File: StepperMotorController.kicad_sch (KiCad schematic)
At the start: 16 parts, among them J1 Conn_01x04, J2 Conn_01x04, J3 Conn_01x08, J4 Conn_01x02, M1 Mounting_Hole, M2 Mounting_Hole, M3 Mounting_Hole, M4 Mounting_Hole, U1 ACS725xLCTR-10AU

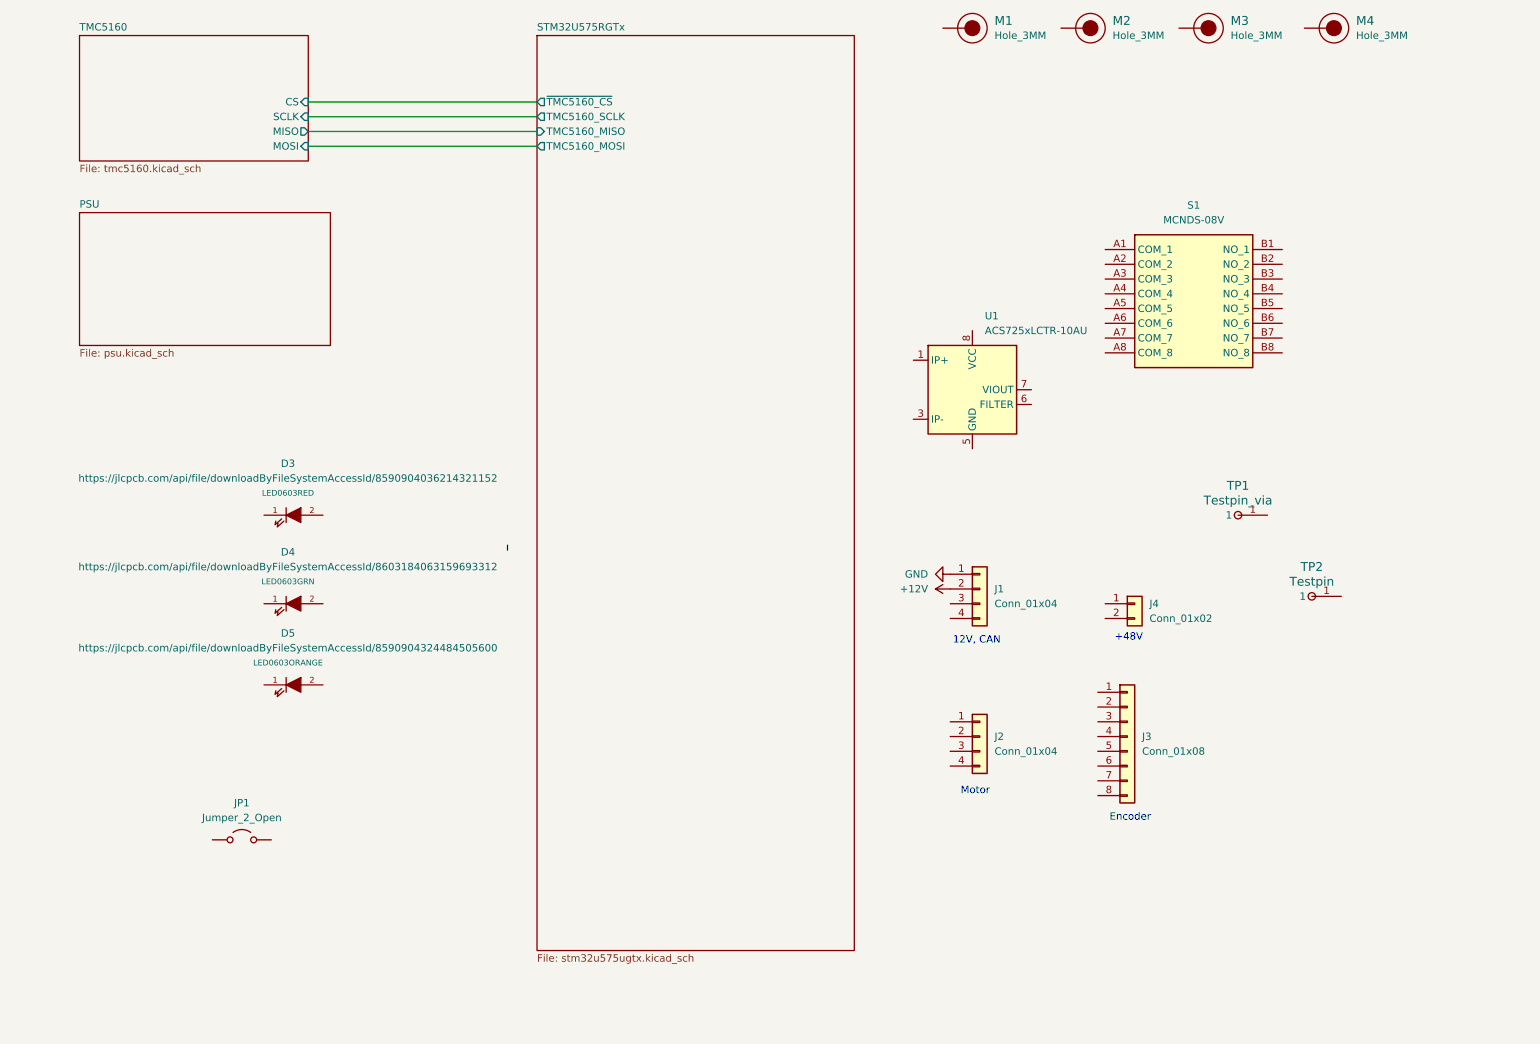
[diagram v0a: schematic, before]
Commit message: PCB 3mm free space around edges, 9pin dipswitch, re-arragnged components
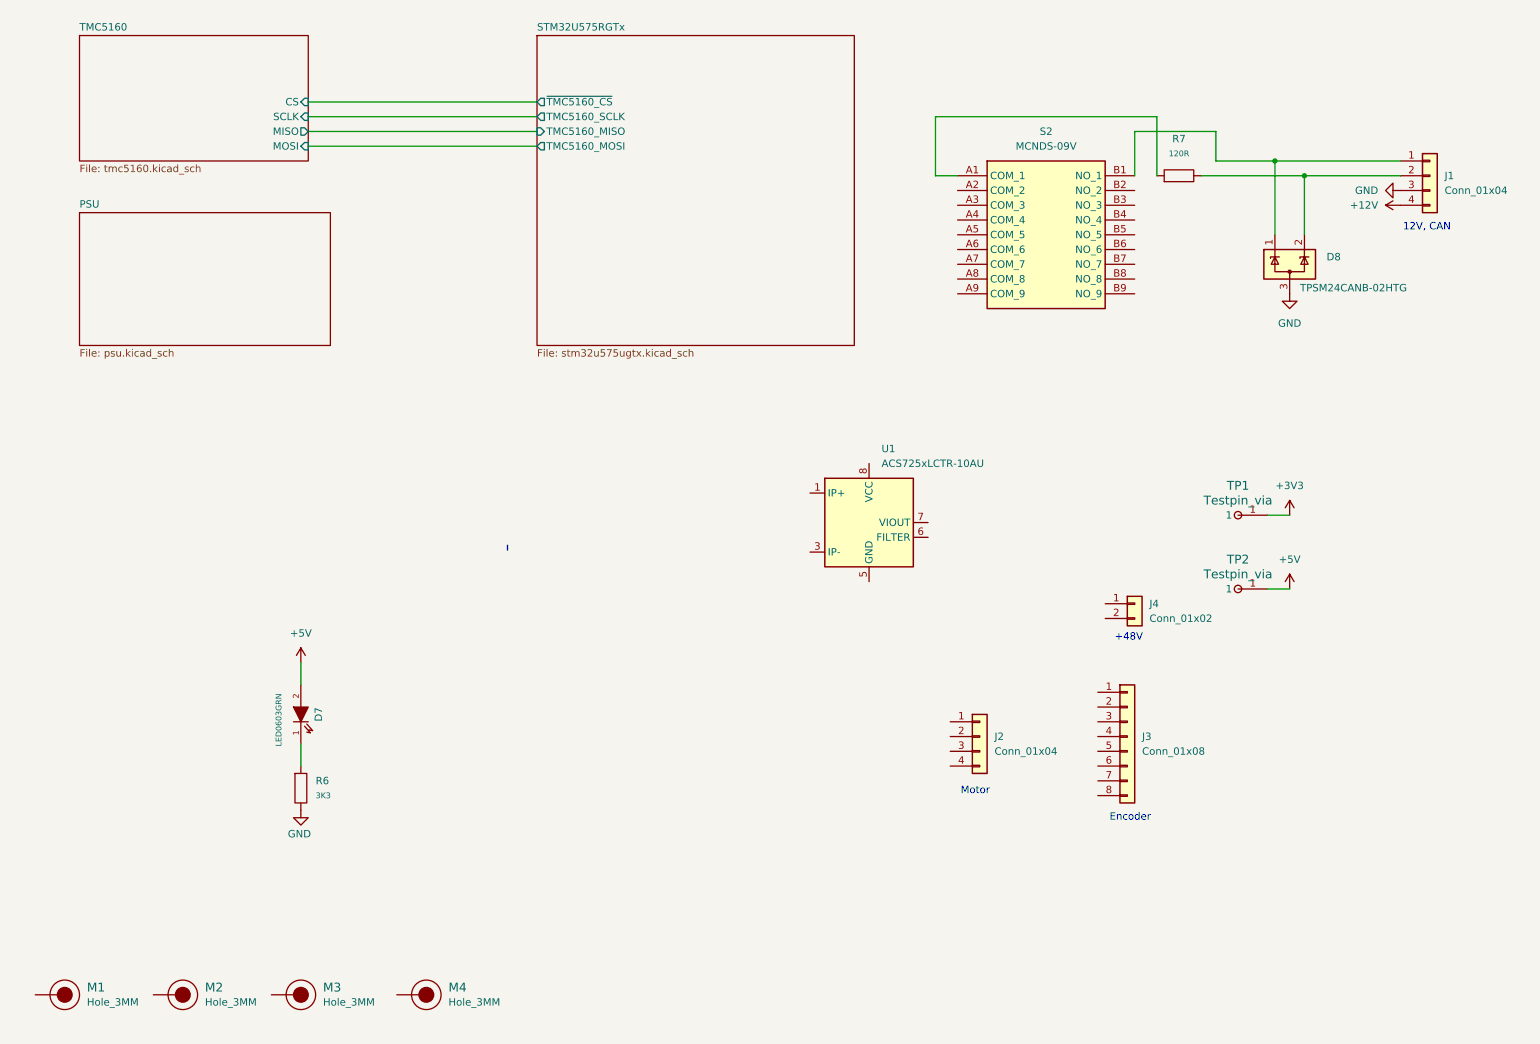
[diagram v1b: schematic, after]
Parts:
- removed D3: LED0603RED_APT1608EC, D&R_Discrete:LED_0603_1608Metric, symbol Doggen:LED0603RED_APT1608EC
- removed D4: LED0603GRN_APT1608ZGC, D&R_Discrete:LED_0603_1608Metric, symbol Doggen:LED0603GRN_APT1608ZGC
- removed D5: LED0603ORANGE_APT1608SECK, D&R_Discrete:LED_0603_1608Metric, symbol Doggen:LED0603ORANGE_APT1608SECK
- removed JP1: Jumper_2_Open, Connector_PinHeader_2.54mm:PinHeader_1x02_P2.54mm_Vertical, symbol Jumper:Jumper_2_Open
- removed S1: MCNDS-08V, Doggen:MCNDS08V, symbol Doggen:MCNDS-08V
- removed TP2: Testpin, D&R_Other:TP1mm, symbol D&R_other:Testpin
- added D7: LED0603GRN_APT1608ZGC, D&R_Discrete:LED_0603_1608Metric, symbol Doggen:LED0603GRN_APT1608ZGC
- added D8: TPSM24CANB-02HTG, Package_TO_SOT_SMD:SOT-23-3, symbol Doggen:TPSM24CANB-02HTG
- added R6: 3K3#0603, D&R_Passive:R_0603, symbol D&R_Passive:3K3#0603
- added R7: 120R#0603, D&R_Passive:R_0603, symbol D&R_Passive:120R#0603
- added S2: MCNDS-09V, MCNDS09V, symbol Doggen:MCNDS-09V
- added TP2: Testpin_via, D&R_Other:Testpoint_Via, symbol D&R_other:Testpin_via
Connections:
- net +12V: now also J1.4 (Pin_4); no longer J1.2 (Pin_2)
- net GND: now also J1.3 (Pin_3), D8.3 (A), R6.2; no longer J1.1 (Pin_1)
- net +3V3: now reaches TP1.1
- new net: D8.1 (K), J1.1 (Pin_1), S2.B1 (NO_1)
- new net: D8.2 (K), J1.2 (Pin_2), R7.2
- new net: D7.1 (K), R6.1
- new net: R7.1, S2.A1 (COM_1)
- new net +5V: D7.2 (A), TP2.1
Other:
- moved on the sheet: J1, M1, M2, M3, M4, U1

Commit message: updated hierarchical sheets
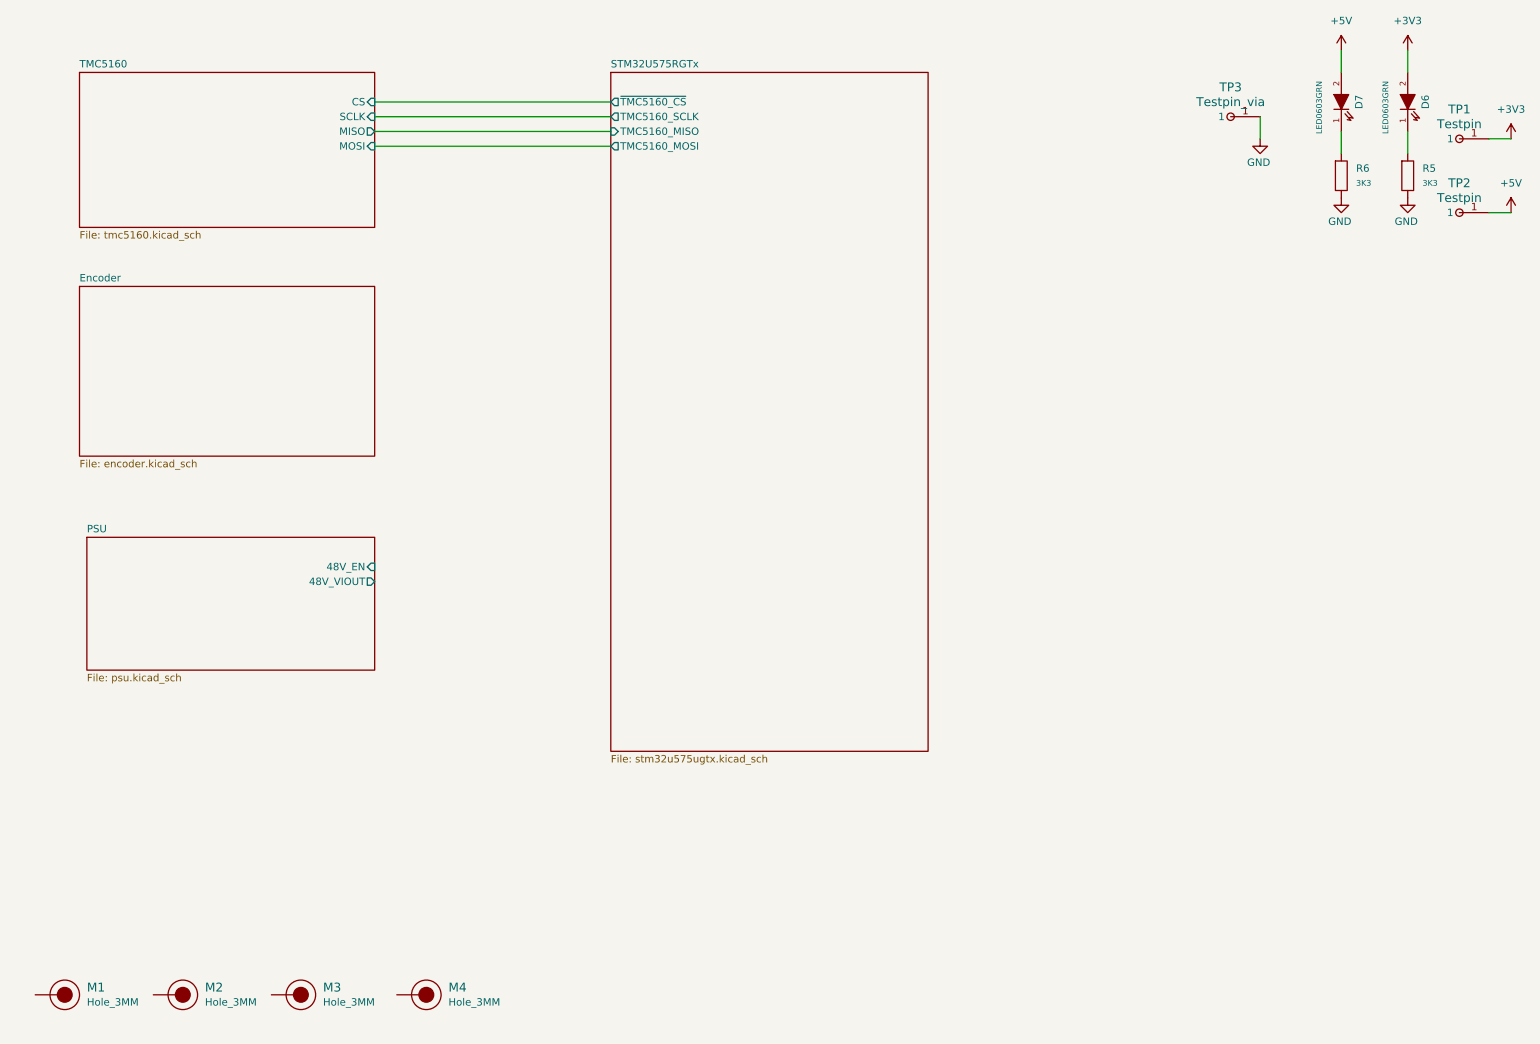
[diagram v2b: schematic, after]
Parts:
- removed D8: TPSM24CANB-02HTG, Package_TO_SOT_SMD:SOT-23-3, symbol Doggen:TPSM24CANB-02HTG
- removed J1, J2: Conn_01x04, Connector_Phoenix_MC:PhoenixContact_MCV_1,5_4-G-3.81_1x04_P3.81mm_Vertical, symbol Connector_Generic:Conn_01x04
- removed J3: Conn_01x08, Connector_Phoenix_MC:PhoenixContact_MCV_1,5_8-G-3.81_1x08_P3.81mm_Vertical, symbol Connector_Generic:Conn_01x08
- removed J4: Conn_01x02, Connector_Phoenix_MC:PhoenixContact_MCV_1,5_2-G-3.81_1x02_P3.81mm_Vertical, symbol Connector_Generic:Conn_01x02
- removed R7: 120R#0603, D&R_Passive:R_0603, symbol D&R_Passive:120R#0603
- removed S2: MCNDS-09V, MCNDS09V, symbol Doggen:MCNDS-09V
- removed TP1, TP2: Testpin_via, D&R_Other:Testpoint_Via, symbol D&R_other:Testpin_via
- removed U1: ACS725xLCTR-10AU, Package_SO:SOIC-8_3.9x4.9mm_P1.27mm, symbol Sensor_Current:ACS725xLCTR-10AU
- added D6: LED0603GRN_APT1608ZGC, D&R_Discrete:LED_0603_1608Metric, symbol Doggen:LED0603GRN_APT1608ZGC
- added R5: 3K3#0603, D&R_Passive:R_0603, symbol D&R_Passive:3K3#0603
- added TP1, TP2: Testpin, D&R_Other:TP1mm, symbol D&R_other:Testpin
- added TP3: Testpin_via, D&R_Other:Testpoint_Via, symbol D&R_other:Testpin_via
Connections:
- net +3V3: now also D6.2 (A), TP1.1
- net +5V: now also TP2.1
- net GND: now also R5.2, TP3.1
- new net: D6.1 (K), R5.1
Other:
- added sheet Encoder (encoder.kicad_sch)
- sheet PSU ports: added 48V_EN, 48V_VIOUT; removed none
- note removed: "+48V"
- note removed: "12V, CAN"
- note removed: "Encoder"
- note removed: "Motor"
- moved on the sheet: D7, R6

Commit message: PCB Finished, only have to check LED's
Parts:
- removed TP3: Testpin_via, D&R_Other:Testpoint_Via, symbol D&R_other:Testpin_via
- added R47, R52, R58, R59, R60, R61: 47R#0603, D&R_Passive:R_0603, symbol D&R_Passive:47R#0603
- renumbered D7 to D1, D6 to D2, R6 to R1, R5 to R2, TP1 to TP2, TP2 to TP3
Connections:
- net GND: now also M1.1, M2.1, M3.1, M4.1
- new net Encoder/ENC_A: R47.1, R59.2
- new net Encoder/ENC_B: R52.1, R60.2
- new net Encoder/ENC_Z: R58.1, R61.2
- new net STM32U575RGTx/ENC_A: R47.2
- new net STM32U575RGTx/ENC_B: R52.2
- new net STM32U575RGTx/ENC_Z: R58.2
- new net TMC5160/ENC_A: R59.1
- new net TMC5160/ENC_B: R60.1
- new net TMC5160/ENC_Z: R61.1
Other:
- sheet Encoder ports: added ENC_A, ENC_B, ENC_Z; removed none
- sheet STM32U575RGTx ports: added 48V_EN, 48V_VIOUT, ENC_A, ENC_B, ENC_Z, REFL_OUT, REFR_OUT, TMC5160_EN; removed none
- sheet TMC5160 ports: added ENC_A, ENC_B, ENC_Z, REFL_IN, REFR_IN, ~{CS}, ~{DRV_EN}; removed CS
- company: (none) -> Doggen Engineering
- title: (none) -> Power Supply
- moved on the sheet: M1, M2, M3, M4
